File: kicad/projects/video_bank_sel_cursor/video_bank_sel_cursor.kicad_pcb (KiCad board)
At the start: 2 copper layers, 203.2 x 97.8 mm, 28 parts, among them J1 peripheral_addr_bus_connector, J2 peripheral_aux_connector, J3 peripheral_membank_connector, J4 Conn_01x16_Socket, J5 Conn_01x16_Socket, J6 Conn_01x16_Socket, J7 Conn_01x16_Socket, U1 74HC245, U10 74HC10, U11 74HC377, U12 74HC377, U13 74HC04, U14 74HC245, U15 74HC245, U2 74HC245, U3 74HC245, U4 74HC245, U5 74HC245, U6 74HC245, U7 74HC245, U8 74HC245, U9 74HC10

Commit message: Add music planning and some extra work planning video card layouts.
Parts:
- removed J6: Conn_01x16_Socket, Connector_PinSocket_2.54mm:PinSocket_1x16_P2.54mm_Horizontal
- moved U11 2.54 mm to (188.0, 124.5)
- moved U14 2.54 mm to (246.4, 124.5)
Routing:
- net unconnected-(U12-Q7-Pad19): track 14.9 -> 16.2 mm
- net unconnected-(U12-Q3-Pad9): track 16.0 -> 17.2 mm
- net unconnected-(U12-Q1-Pad5): track 16.1 -> 17.2 mm
- net unconnected-(U12-Q5-Pad15): track 16.0 -> 17.2 mm
- net unconnected-(U12-Q0-Pad2): track 17.2 -> 18.3 mm
- net unconnected-(U12-Q2-Pad6): track 17.0 -> 17.9 mm

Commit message: Bit more tweaking and fleshing out of video circuits.
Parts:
- removed U13: 74HC04, Package_DIP:DIP-14_W7.62mm_Socket
- added C10: C, Capacitor_THT:C_Disc_D5.0mm_W2.5mm_P5.00mm, F.Cu at (185.4, 133.3)
- added C11: C, Capacitor_THT:C_Disc_D5.0mm_W2.5mm_P5.00mm, F.Cu at (172.7, 133.3)
- added C12: C, Capacitor_THT:C_Disc_D5.0mm_W2.5mm_P5.00mm, F.Cu at (200.7, 133.3)
- added C13: C, Capacitor_THT:C_Disc_D5.0mm_W2.5mm_P5.00mm, F.Cu at (213.4, 133.3)
- added C14: C, Capacitor_THT:C_Disc_D5.0mm_W2.5mm_P5.00mm, F.Cu at (226.1, 128.3)
- added C15: C, Capacitor_THT:C_Disc_D5.0mm_W2.5mm_P5.00mm, F.Cu at (238.8, 128.3)
- added C2: C, Capacitor_THT:C_Disc_D5.0mm_W2.5mm_P5.00mm, F.Cu at (-14.4, 59.5)
- added C3: C, Capacitor_THT:C_Disc_D5.0mm_W2.5mm_P5.00mm, F.Cu at (-14.4, 63.6)
- added C4: C, Capacitor_THT:C_Disc_D5.0mm_W2.5mm_P5.00mm, F.Cu at (-14.4, 67.6)
- added C5: C, Capacitor_THT:C_Disc_D5.0mm_W2.5mm_P5.00mm, F.Cu at (-14.4, 71.7)
- added C6: C, Capacitor_THT:C_Disc_D5.0mm_W2.5mm_P5.00mm, F.Cu at (-14.4, 75.7)
- added C7: C, Capacitor_THT:C_Disc_D5.0mm_W2.5mm_P5.00mm, F.Cu at (-14.4, 79.8)
- added C8: C, Capacitor_THT:C_Disc_D5.0mm_W2.5mm_P5.00mm, F.Cu at (147.3, 133.3)
- added C9: C, Capacitor_THT:C_Disc_D5.0mm_W2.5mm_P5.00mm, F.Cu at (160.0, 133.3)
- moved U2 127.7 mm to (221.0, 124.5), turned to 180 degrees
- moved U6 112.1 mm to (208.3, 124.5), turned to 180 degrees
- moved U7 111.1 mm to (99.1, 104.1), turned to 90 degrees
- moved J4 109.2 mm to (139.7, 61.0)
- moved J7 106.7 mm to (248.9, 61.0)
- moved U3 67.1 mm to (99.1, 91.4), turned to 90 degrees
- moved U12 53.3 mm to (180.3, 124.5)
- moved U4 53.3 mm to (167.6, 124.5)
- moved U15 50.8 mm to (193.0, 124.5)
- moved U11 45.7 mm to (233.7, 124.5)
- moved U8 17.8 mm to (154.9, 124.5)
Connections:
- J1 pad 1: /DATA_BUS_00 -> /DATA_BUS_0
- J1 pad 10: /DATA_BUS_09 -> unconnected-(J1-D_09-Pad10)
- J1 pad 11: /DATA_BUS_10 -> unconnected-(J1-D_10-Pad11)
- J1 pad 12: /DATA_BUS_11 -> unconnected-(J1-D_11-Pad12)
- J1 pad 13: /DATA_BUS_12 -> unconnected-(J1-D_12-Pad13)
- J1 pad 14: /DATA_BUS_13 -> unconnected-(J1-D_13-Pad14)
- J1 pad 15: /DATA_BUS_14 -> unconnected-(J1-D_14-Pad15)
- J1 pad 16: /DATA_BUS_15 -> unconnected-(J1-D_15-Pad16)
- J1 pad 17: /ADDR_BUS_00 -> unconnected-(J1-A_00-Pad17)
- J1 pad 18: /ADDR_BUS_01 -> unconnected-(J1-A_01-Pad18)
- J1 pad 19: /ADDR_BUS_02 -> unconnected-(J1-A_02-Pad19)
- J1 pad 2: /DATA_BUS_01 -> /DATA_BUS_1
- J1 pad 20: /ADDR_BUS_03 -> unconnected-(J1-A_03-Pad20)
- J1 pad 21: /ADDR_BUS_04 -> unconnected-(J1-A_04-Pad21)
- J1 pad 22: /ADDR_BUS_05 -> unconnected-(J1-A_05-Pad22)
- J1 pad 23: /ADDR_BUS_06 -> unconnected-(J1-A_06-Pad23)
- J1 pad 24: /ADDR_BUS_07 -> unconnected-(J1-A_07-Pad24)
- J1 pad 25: /ADDR_BUS_08 -> unconnected-(J1-A_08-Pad25)
- J1 pad 26: /ADDR_BUS_09 -> unconnected-(J1-A_09-Pad26)
- J1 pad 27: /ADDR_BUS_10 -> unconnected-(J1-A_10-Pad27)
- J1 pad 28: /ADDR_BUS_11 -> unconnected-(J1-A_11-Pad28)
- J1 pad 29: /ADDR_BUS_12 -> unconnected-(J1-A_12-Pad29)
- J1 pad 3: /DATA_BUS_02 -> /DATA_BUS_2
- J1 pad 30: /ADDR_BUS_13 -> unconnected-(J1-A_13-Pad30)
- J1 pad 31: /ADDR_BUS_14 -> unconnected-(J1-A_14-Pad31)
- J1 pad 32: /ADDR_BUS_15 -> unconnected-(J1-A_15-Pad32)
- J1 pad 4: /DATA_BUS_03 -> /DATA_BUS_3
- J1 pad 5: /DATA_BUS_04 -> /DATA_BUS_4
- J1 pad 6: /DATA_BUS_05 -> /DATA_BUS_5
- J1 pad 7: /DATA_BUS_06 -> /DATA_BUS_6
- J1 pad 8: /DATA_BUS_07 -> /DATA_BUS_7
- J1 pad 9: /DATA_BUS_08 -> unconnected-(J1-D_08-Pad9)
- J2 pad 10: /RFM -> /MEM_ACT
- J2 pad 12: /WTM -> /~{RFM}/WTM
- J3 pad 1: /BANK_BUS_00 -> unconnected-(J3-B_00-Pad1)
- J3 pad 10: /BANK_BUS_09 -> unconnected-(J3-B_09-Pad10)
- J3 pad 11: /BANK_BUS_10 -> unconnected-(J3-B_10-Pad11)
- J3 pad 12: /BANK_BUS_11 -> unconnected-(J3-B_11-Pad12)
- J3 pad 13: /BANK_BUS_12 -> unconnected-(J3-B_12-Pad13)
- J3 pad 14: /BANK_BUS_13 -> unconnected-(J3-B_13-Pad14)
- J3 pad 15: /BANK_BUS_14 -> unconnected-(J3-B_14-Pad15)
- J3 pad 16: /BANK_BUS_15 -> unconnected-(J3-B_15-Pad16)
- J3 pad 2: /BANK_BUS_01 -> unconnected-(J3-B_01-Pad2)
- J3 pad 3: /BANK_BUS_02 -> unconnected-(J3-B_02-Pad3)
- J3 pad 4: /BANK_BUS_03 -> unconnected-(J3-B_03-Pad4)
- J3 pad 5: /BANK_BUS_04 -> unconnected-(J3-B_04-Pad5)
- J3 pad 6: /BANK_BUS_05 -> unconnected-(J3-B_05-Pad6)
- J3 pad 7: /BANK_BUS_06 -> unconnected-(J3-B_06-Pad7)
- J3 pad 8: /BANK_BUS_07 -> unconnected-(J3-B_07-Pad8)
- J3 pad 9: /BANK_BUS_08 -> unconnected-(J3-B_08-Pad9)
- J4 pad 1: unconnected-(J4-Pin_1-Pad1) -> /EXT_COL_0
- J4 pad 10: unconnected-(J4-Pin_10-Pad10) -> /EXT_ROW_1
- J4 pad 11: unconnected-(J4-Pin_11-Pad11) -> /EXT_ROW_2
- J4 pad 12: unconnected-(J4-Pin_12-Pad12) -> /EXT_ROW_3
- J4 pad 13: unconnected-(J4-Pin_13-Pad13) -> /EXT_ROW_4
- J4 pad 14: unconnected-(J4-Pin_14-Pad14) -> /EXT_ROW_5
- J4 pad 15: unconnected-(J4-Pin_15-Pad15) -> /EXT_ROW_6
- J4 pad 16: unconnected-(J4-Pin_16-Pad16) -> /EXT_ROW_7
- J4 pad 2: unconnected-(J4-Pin_2-Pad2) -> /EXT_COL_1
- J4 pad 3: unconnected-(J4-Pin_3-Pad3) -> /EXT_COL_2
- J4 pad 4: unconnected-(J4-Pin_4-Pad4) -> /EXT_COL_3
- J4 pad 5: unconnected-(J4-Pin_5-Pad5) -> /EXT_COL_4
- J4 pad 6: unconnected-(J4-Pin_6-Pad6) -> /EXT_COL_5
- J4 pad 7: unconnected-(J4-Pin_7-Pad7) -> /EXT_COL_6
- J4 pad 8: unconnected-(J4-Pin_8-Pad8) -> /EXT_COL_7
- J4 pad 9: unconnected-(J4-Pin_9-Pad9) -> /EXT_ROW_0
- J5 pad 1: unconnected-(J5-Pin_1-Pad1) -> /OUT_A_COL_0
- J5 pad 10: unconnected-(J5-Pin_10-Pad10) -> /OUT_A_ROW_1
- J5 pad 11: unconnected-(J5-Pin_11-Pad11) -> /OUT_A_ROW_2
- J5 pad 12: unconnected-(J5-Pin_12-Pad12) -> /OUT_A_ROW_3
- J5 pad 13: unconnected-(J5-Pin_13-Pad13) -> /OUT_A_ROW_4
- J5 pad 14: unconnected-(J5-Pin_14-Pad14) -> /OUT_A_ROW_5
- J5 pad 15: unconnected-(J5-Pin_15-Pad15) -> /OUT_A_ROW_6
- J5 pad 16: unconnected-(J5-Pin_16-Pad16) -> /OUT_A_ROW_7
- J5 pad 2: unconnected-(J5-Pin_2-Pad2) -> /OUT_A_COL_1
- J5 pad 3: unconnected-(J5-Pin_3-Pad3) -> /OUT_A_COL_2
- J5 pad 4: unconnected-(J5-Pin_4-Pad4) -> /OUT_A_COL_3
- J5 pad 5: unconnected-(J5-Pin_5-Pad5) -> /OUT_A_COL_4
- J5 pad 6: unconnected-(J5-Pin_6-Pad6) -> /OUT_A_COL_5
- J5 pad 7: unconnected-(J5-Pin_7-Pad7) -> /OUT_A_COL_6
- J5 pad 8: unconnected-(J5-Pin_8-Pad8) -> /OUT_A_COL_7
- J5 pad 9: unconnected-(J5-Pin_9-Pad9) -> /OUT_A_ROW_0
- J7 pad 1: unconnected-(J7-Pin_1-Pad1) -> /OUT_B_COL_0
- J7 pad 10: unconnected-(J7-Pin_10-Pad10) -> /OUT_B_ROW_1
- J7 pad 11: unconnected-(J7-Pin_11-Pad11) -> /OUT_B_ROW_2
- J7 pad 12: unconnected-(J7-Pin_12-Pad12) -> /OUT_B_ROW_3
- J7 pad 13: unconnected-(J7-Pin_13-Pad13) -> /OUT_B_ROW_4
- J7 pad 14: unconnected-(J7-Pin_14-Pad14) -> /OUT_B_ROW_5
- J7 pad 15: unconnected-(J7-Pin_15-Pad15) -> /OUT_B_ROW_6
- J7 pad 16: unconnected-(J7-Pin_16-Pad16) -> /OUT_B_ROW_7
- J7 pad 2: unconnected-(J7-Pin_2-Pad2) -> /OUT_B_COL_1
- J7 pad 3: unconnected-(J7-Pin_3-Pad3) -> /OUT_B_COL_2
- J7 pad 4: unconnected-(J7-Pin_4-Pad4) -> /OUT_B_COL_3
- J7 pad 5: unconnected-(J7-Pin_5-Pad5) -> /OUT_B_COL_4
- J7 pad 6: unconnected-(J7-Pin_6-Pad6) -> /OUT_B_COL_5
- J7 pad 7: unconnected-(J7-Pin_7-Pad7) -> /OUT_B_COL_6
- J7 pad 8: unconnected-(J7-Pin_8-Pad8) -> /OUT_B_COL_7
- J7 pad 9: unconnected-(J7-Pin_9-Pad9) -> /OUT_B_ROW_0
- U1 pad 10: unconnected-(U1-GND-Pad10) -> GND
- U1 pad 11: unconnected-(U1-B8-Pad11) -> /OUT_A_ROW_7
- U1 pad 12: unconnected-(U1-B7-Pad12) -> /OUT_A_ROW_6
- U1 pad 13: unconnected-(U1-B6-Pad13) -> /OUT_A_ROW_5
- U1 pad 14: unconnected-(U1-B5-Pad14) -> /OUT_A_ROW_4
- U1 pad 15: unconnected-(U1-B4-Pad15) -> /OUT_A_ROW_3
- U1 pad 16: unconnected-(U1-B3-Pad16) -> /OUT_A_ROW_2
- U1 pad 17: unconnected-(U1-B2-Pad17) -> /OUT_A_ROW_1
- U1 pad 18: unconnected-(U1-B1-Pad18) -> /OUT_A_ROW_0
- U1 pad 19: unconnected-(U1-~{OE}-Pad19) -> /~{BANK_SEL}
- U1 pad 2: unconnected-(U1-A1-Pad2) -> /EXT_ROW_0
- U1 pad 20: unconnected-(U1-VCC-Pad20) -> VCC
- U1 pad 3: unconnected-(U1-A2-Pad3) -> /EXT_ROW_1
- U1 pad 4: unconnected-(U1-A3-Pad4) -> /EXT_ROW_2
- U1 pad 5: unconnected-(U1-A3-Pad5) -> /EXT_ROW_3
- U1 pad 6: unconnected-(U1-A5-Pad6) -> /EXT_ROW_4
- U1 pad 7: unconnected-(U1-A6-Pad7) -> /EXT_ROW_5
- U1 pad 8: unconnected-(U1-A7-Pad8) -> /EXT_ROW_6
- U1 pad 9: unconnected-(U1-A8-Pad9) -> /EXT_ROW_7
- U10 pad 1: unconnected-(U10-Pad1) -> /CURSOR_ROW_ADDRESSED
- U10 pad 10: unconnected-(U10-Pad10) -> VCC
- U10 pad 11: unconnected-(U10-Pad11) -> VCC
- U10 pad 12: unconnected-(U10-Pad12) -> /~{CURSOR_ROW_WTM}
- U10 pad 13: unconnected-(U10-Pad13) -> /~{RFM}/WTM
- U10 pad 14: unconnected-(U10D-VCC-Pad14) -> VCC
- U10 pad 2: unconnected-(U10-Pad2) -> /MEM_ACT
- U10 pad 3: unconnected-(U10-Pad3) -> /CURSOR_COL_ADDRESSED
- U10 pad 4: unconnected-(U10-Pad4) -> /MEM_ACT
- U10 pad 5: unconnected-(U10-Pad5) -> /RFM/~{WTM}
- U10 pad 6: unconnected-(U10-Pad6) -> /~{CURSOR_COL_RFM}
- U10 pad 7: unconnected-(U10D-GND-Pad7) -> GND
- U10 pad 8: unconnected-(U10-Pad8) -> /~{BANK_SEL}
- U10 pad 9: unconnected-(U10-Pad9) -> /BANK_SEL
- U11 pad 1: unconnected-(U11-~{E}-Pad1) -> /~{CURSOR_ROW_WTM}
- U11 pad 10: unconnected-(U11-GND-Pad10) -> GND
- U11 pad 11: unconnected-(U11-CP-Pad11) -> /DATA_CLK
- U11 pad 12: unconnected-(U11-Q4-Pad12) -> /CURS_ROW_4
- U11 pad 13: unconnected-(U11-D4-Pad13) -> /DATA_BUS_4
- U11 pad 14: unconnected-(U11-D5-Pad14) -> /DATA_BUS_5
- U11 pad 15: unconnected-(U11-Q5-Pad15) -> /CURS_ROW_5
- U11 pad 16: unconnected-(U11-Q6-Pad16) -> /CURS_ROW_6
- U11 pad 17: unconnected-(U11-D6-Pad17) -> /DATA_BUS_6
- U11 pad 18: unconnected-(U11-D7-Pad18) -> /DATA_BUS_7
- U11 pad 19: unconnected-(U11-Q7-Pad19) -> /CURS_ROW_7
- U11 pad 2: unconnected-(U11-Q0-Pad2) -> /CURS_ROW_0
- U11 pad 20: unconnected-(U11-VCC-Pad20) -> VCC
- U11 pad 3: unconnected-(U11-D0-Pad3) -> /DATA_BUS_0
- U11 pad 4: unconnected-(U11-D1-Pad4) -> /DATA_BUS_1
- U11 pad 5: unconnected-(U11-Q1-Pad5) -> /CURS_ROW_1
- U11 pad 6: unconnected-(U11-Q2-Pad6) -> /CURS_ROW_2
- U11 pad 7: unconnected-(U11-D2-Pad7) -> /DATA_BUS_2
- U11 pad 8: unconnected-(U11-D3-Pad8) -> /DATA_BUS_3
- U11 pad 9: unconnected-(U11-Q3-Pad9) -> /CURS_ROW_3
- U12 pad 1: unconnected-(U12-~{E}-Pad1) -> /~{CURSOR_COL_WTM}
- U12 pad 10: unconnected-(U12-GND-Pad10) -> GND
- U12 pad 11: unconnected-(U12-CP-Pad11) -> /DATA_CLK
- U12 pad 12: unconnected-(U12-Q4-Pad12) -> /CURS_COL_4
- U12 pad 13: unconnected-(U12-D4-Pad13) -> /DATA_BUS_4
- U12 pad 14: unconnected-(U12-D5-Pad14) -> /DATA_BUS_5
- U12 pad 15: unconnected-(U12-Q5-Pad15) -> /CURS_COL_5
- U12 pad 16: unconnected-(U12-Q6-Pad16) -> /CURS_COL_6
- U12 pad 17: unconnected-(U12-D6-Pad17) -> /DATA_BUS_6
- U12 pad 18: unconnected-(U12-D7-Pad18) -> /DATA_BUS_7
- U12 pad 19: unconnected-(U12-Q7-Pad19) -> /CURS_COL_7
- U12 pad 2: unconnected-(U12-Q0-Pad2) -> /CURS_COL_0
- U12 pad 20: unconnected-(U12-VCC-Pad20) -> VCC
- U12 pad 3: unconnected-(U12-D0-Pad3) -> /DATA_BUS_0
- U12 pad 4: unconnected-(U12-D1-Pad4) -> /DATA_BUS_1
- U12 pad 5: unconnected-(U12-Q1-Pad5) -> /CURS_COL_1
- U12 pad 6: unconnected-(U12-Q2-Pad6) -> /CURS_COL_2
- U12 pad 7: unconnected-(U12-D2-Pad7) -> /DATA_BUS_2
- U12 pad 8: unconnected-(U12-D3-Pad8) -> /DATA_BUS_3
- U12 pad 9: unconnected-(U12-Q3-Pad9) -> /CURS_COL_3
- U14 pad 10: unconnected-(U14-GND-Pad10) -> GND
- U14 pad 11: unconnected-(U14-B8-Pad11) -> /DATA_BUS_7
- U14 pad 12: unconnected-(U14-B7-Pad12) -> /DATA_BUS_6
- U14 pad 13: unconnected-(U14-B6-Pad13) -> /DATA_BUS_5
- U14 pad 14: unconnected-(U14-B5-Pad14) -> /DATA_BUS_4
- U14 pad 15: unconnected-(U14-B4-Pad15) -> /DATA_BUS_3
- U14 pad 16: unconnected-(U14-B3-Pad16) -> /DATA_BUS_2
- U14 pad 17: unconnected-(U14-B2-Pad17) -> /DATA_BUS_1
- U14 pad 18: unconnected-(U14-B1-Pad18) -> /DATA_BUS_0
- U14 pad 19: unconnected-(U14-~{OE}-Pad19) -> /~{CURSOR_ROW_RFM}
- U14 pad 2: unconnected-(U14-A1-Pad2) -> /CURS_ROW_0
- U14 pad 20: unconnected-(U14-VCC-Pad20) -> VCC
- U14 pad 3: unconnected-(U14-A2-Pad3) -> /CURS_ROW_1
- U14 pad 4: unconnected-(U14-A3-Pad4) -> /CURS_ROW_2
- U14 pad 5: unconnected-(U14-A3-Pad5) -> /CURS_ROW_3
- U14 pad 6: unconnected-(U14-A5-Pad6) -> /CURS_ROW_4
- U14 pad 7: unconnected-(U14-A6-Pad7) -> /CURS_ROW_5
- U14 pad 8: unconnected-(U14-A7-Pad8) -> /CURS_ROW_6
- U14 pad 9: unconnected-(U14-A8-Pad9) -> /CURS_ROW_7
- U15 pad 10: unconnected-(U15-GND-Pad10) -> GND
- U15 pad 11: unconnected-(U15-B8-Pad11) -> /DATA_BUS_7
- U15 pad 12: unconnected-(U15-B7-Pad12) -> /DATA_BUS_6
- U15 pad 13: unconnected-(U15-B6-Pad13) -> /DATA_BUS_5
- U15 pad 14: unconnected-(U15-B5-Pad14) -> /DATA_BUS_4
- U15 pad 15: unconnected-(U15-B4-Pad15) -> /DATA_BUS_3
- U15 pad 16: unconnected-(U15-B3-Pad16) -> /DATA_BUS_2
- U15 pad 17: unconnected-(U15-B2-Pad17) -> /DATA_BUS_1
- U15 pad 18: unconnected-(U15-B1-Pad18) -> /DATA_BUS_0
- U15 pad 19: unconnected-(U15-~{OE}-Pad19) -> /~{CURSOR_COL_RFM}
- U15 pad 2: unconnected-(U15-A1-Pad2) -> /CURS_COL_0
- U15 pad 20: unconnected-(U15-VCC-Pad20) -> VCC
- U15 pad 3: unconnected-(U15-A2-Pad3) -> /CURS_COL_1
- U15 pad 4: unconnected-(U15-A3-Pad4) -> /CURS_COL_2
- U15 pad 5: unconnected-(U15-A3-Pad5) -> /CURS_COL_3
- U15 pad 6: unconnected-(U15-A5-Pad6) -> /CURS_COL_4
- U15 pad 7: unconnected-(U15-A6-Pad7) -> /CURS_COL_5
- U15 pad 8: unconnected-(U15-A7-Pad8) -> /CURS_COL_6
- U15 pad 9: unconnected-(U15-A8-Pad9) -> /CURS_COL_7
- U2 pad 10: unconnected-(U2-GND-Pad10) -> GND
- U2 pad 11: unconnected-(U2-B8-Pad11) -> /OUT_A_ROW_7
- U2 pad 12: unconnected-(U2-B7-Pad12) -> /OUT_A_ROW_6
- U2 pad 13: unconnected-(U2-B6-Pad13) -> /OUT_A_ROW_5
- U2 pad 14: unconnected-(U2-B5-Pad14) -> /OUT_A_ROW_4
- U2 pad 15: unconnected-(U2-B4-Pad15) -> /OUT_A_ROW_3
- U2 pad 16: unconnected-(U2-B3-Pad16) -> /OUT_A_ROW_2
- U2 pad 17: unconnected-(U2-B2-Pad17) -> /OUT_A_ROW_1
- U2 pad 18: unconnected-(U2-B1-Pad18) -> /OUT_A_ROW_0
- U2 pad 19: unconnected-(U2-~{OE}-Pad19) -> /BANK_SEL
- U2 pad 2: unconnected-(U2-A1-Pad2) -> /CURS_ROW_0
- U2 pad 20: unconnected-(U2-VCC-Pad20) -> VCC
- U2 pad 3: unconnected-(U2-A2-Pad3) -> /CURS_ROW_1
- U2 pad 4: unconnected-(U2-A3-Pad4) -> /CURS_ROW_2
- U2 pad 5: unconnected-(U2-A3-Pad5) -> /CURS_ROW_3
- U2 pad 6: unconnected-(U2-A5-Pad6) -> /CURS_ROW_4
- U2 pad 7: unconnected-(U2-A6-Pad7) -> /CURS_ROW_5
- U2 pad 8: unconnected-(U2-A7-Pad8) -> /CURS_ROW_6
- U2 pad 9: unconnected-(U2-A8-Pad9) -> /CURS_ROW_7
- U3 pad 10: unconnected-(U3-GND-Pad10) -> GND
- U3 pad 11: unconnected-(U3-B8-Pad11) -> /OUT_A_COL_7
- U3 pad 12: unconnected-(U3-B7-Pad12) -> /OUT_A_COL_6
- U3 pad 13: unconnected-(U3-B6-Pad13) -> /OUT_A_COL_5
- U3 pad 14: unconnected-(U3-B5-Pad14) -> /OUT_A_COL_4
- U3 pad 15: unconnected-(U3-B4-Pad15) -> /OUT_A_COL_3
- U3 pad 16: unconnected-(U3-B3-Pad16) -> /OUT_A_COL_2
- U3 pad 17: unconnected-(U3-B2-Pad17) -> /OUT_A_COL_1
- U3 pad 18: unconnected-(U3-B1-Pad18) -> /OUT_A_COL_0
- U3 pad 19: unconnected-(U3-~{OE}-Pad19) -> /~{BANK_SEL}
- U3 pad 2: unconnected-(U3-A1-Pad2) -> /EXT_COL_0
- U3 pad 20: unconnected-(U3-VCC-Pad20) -> VCC
- U3 pad 3: unconnected-(U3-A2-Pad3) -> /EXT_COL_1
- U3 pad 4: unconnected-(U3-A3-Pad4) -> /EXT_COL_2
- U3 pad 5: unconnected-(U3-A3-Pad5) -> /EXT_COL_3
- U3 pad 6: unconnected-(U3-A5-Pad6) -> /EXT_COL_4
- U3 pad 7: unconnected-(U3-A6-Pad7) -> /EXT_COL_5
- U3 pad 8: unconnected-(U3-A7-Pad8) -> /EXT_COL_6
- U3 pad 9: unconnected-(U3-A8-Pad9) -> /EXT_COL_7
- U4 pad 10: unconnected-(U4-GND-Pad10) -> GND
- U4 pad 11: unconnected-(U4-B8-Pad11) -> /OUT_A_COL_7
- U4 pad 12: unconnected-(U4-B7-Pad12) -> /OUT_A_COL_6
- U4 pad 13: unconnected-(U4-B6-Pad13) -> /OUT_A_COL_5
- U4 pad 14: unconnected-(U4-B5-Pad14) -> /OUT_A_COL_4
- U4 pad 15: unconnected-(U4-B4-Pad15) -> /OUT_A_COL_3
- U4 pad 16: unconnected-(U4-B3-Pad16) -> /OUT_A_COL_2
- U4 pad 17: unconnected-(U4-B2-Pad17) -> /OUT_A_COL_1
- U4 pad 18: unconnected-(U4-B1-Pad18) -> /OUT_A_COL_0
- U4 pad 19: unconnected-(U4-~{OE}-Pad19) -> /BANK_SEL
- U4 pad 2: unconnected-(U4-A1-Pad2) -> /CURS_COL_0
- U4 pad 20: unconnected-(U4-VCC-Pad20) -> VCC
- U4 pad 3: unconnected-(U4-A2-Pad3) -> /CURS_COL_1
- U4 pad 4: unconnected-(U4-A3-Pad4) -> /CURS_COL_2
- U4 pad 5: unconnected-(U4-A3-Pad5) -> /CURS_COL_3
- U4 pad 6: unconnected-(U4-A5-Pad6) -> /CURS_COL_4
- U4 pad 7: unconnected-(U4-A6-Pad7) -> /CURS_COL_5
- U4 pad 8: unconnected-(U4-A7-Pad8) -> /CURS_COL_6
- U4 pad 9: unconnected-(U4-A8-Pad9) -> /CURS_COL_7
- U5 pad 10: unconnected-(U5-GND-Pad10) -> GND
- U5 pad 11: unconnected-(U5-B8-Pad11) -> /OUT_B_ROW_7
- U5 pad 12: unconnected-(U5-B7-Pad12) -> /OUT_B_ROW_6
- U5 pad 13: unconnected-(U5-B6-Pad13) -> /OUT_B_ROW_5
- U5 pad 14: unconnected-(U5-B5-Pad14) -> /OUT_B_ROW_4
- U5 pad 15: unconnected-(U5-B4-Pad15) -> /OUT_B_ROW_3
- U5 pad 16: unconnected-(U5-B3-Pad16) -> /OUT_B_ROW_2
- U5 pad 17: unconnected-(U5-B2-Pad17) -> /OUT_B_ROW_1
- U5 pad 18: unconnected-(U5-B1-Pad18) -> /OUT_B_ROW_0
- U5 pad 19: unconnected-(U5-~{OE}-Pad19) -> /BANK_SEL
- U5 pad 2: unconnected-(U5-A1-Pad2) -> /EXT_ROW_0
- U5 pad 20: unconnected-(U5-VCC-Pad20) -> VCC
- U5 pad 3: unconnected-(U5-A2-Pad3) -> /EXT_ROW_1
- U5 pad 4: unconnected-(U5-A3-Pad4) -> /EXT_ROW_2
- U5 pad 5: unconnected-(U5-A3-Pad5) -> /EXT_ROW_3
- U5 pad 6: unconnected-(U5-A5-Pad6) -> /EXT_ROW_4
- U5 pad 7: unconnected-(U5-A6-Pad7) -> /EXT_ROW_5
- U5 pad 8: unconnected-(U5-A7-Pad8) -> /EXT_ROW_6
- U5 pad 9: unconnected-(U5-A8-Pad9) -> /EXT_ROW_7
- U6 pad 10: unconnected-(U6-GND-Pad10) -> GND
- U6 pad 11: unconnected-(U6-B8-Pad11) -> /OUT_B_ROW_7
- U6 pad 12: unconnected-(U6-B7-Pad12) -> /OUT_B_ROW_6
- U6 pad 13: unconnected-(U6-B6-Pad13) -> /OUT_B_ROW_5
- U6 pad 14: unconnected-(U6-B5-Pad14) -> /OUT_B_ROW_4
- U6 pad 15: unconnected-(U6-B4-Pad15) -> /OUT_B_ROW_3
- U6 pad 16: unconnected-(U6-B3-Pad16) -> /OUT_B_ROW_2
- U6 pad 17: unconnected-(U6-B2-Pad17) -> /OUT_B_ROW_1
- U6 pad 18: unconnected-(U6-B1-Pad18) -> /OUT_B_ROW_0
- U6 pad 19: unconnected-(U6-~{OE}-Pad19) -> /~{BANK_SEL}
- U6 pad 2: unconnected-(U6-A1-Pad2) -> /CURS_ROW_0
- U6 pad 20: unconnected-(U6-VCC-Pad20) -> VCC
- U6 pad 3: unconnected-(U6-A2-Pad3) -> /CURS_ROW_1
- U6 pad 4: unconnected-(U6-A3-Pad4) -> /CURS_ROW_2
- U6 pad 5: unconnected-(U6-A3-Pad5) -> /CURS_ROW_3
- U6 pad 6: unconnected-(U6-A5-Pad6) -> /CURS_ROW_4
- U6 pad 7: unconnected-(U6-A6-Pad7) -> /CURS_ROW_5
- U6 pad 8: unconnected-(U6-A7-Pad8) -> /CURS_ROW_6
- U6 pad 9: unconnected-(U6-A8-Pad9) -> /CURS_ROW_7
- U7 pad 10: unconnected-(U7-GND-Pad10) -> GND
- U7 pad 11: unconnected-(U7-B8-Pad11) -> /OUT_B_COL_7
- U7 pad 12: unconnected-(U7-B7-Pad12) -> /OUT_B_COL_6
- U7 pad 13: unconnected-(U7-B6-Pad13) -> /OUT_B_COL_5
- U7 pad 14: unconnected-(U7-B5-Pad14) -> /OUT_B_COL_4
- U7 pad 15: unconnected-(U7-B4-Pad15) -> /OUT_B_COL_3
- U7 pad 16: unconnected-(U7-B3-Pad16) -> /OUT_B_COL_2
- U7 pad 17: unconnected-(U7-B2-Pad17) -> /OUT_B_COL_1
- U7 pad 18: unconnected-(U7-B1-Pad18) -> /OUT_B_COL_0
- U7 pad 19: unconnected-(U7-~{OE}-Pad19) -> /BANK_SEL
- U7 pad 2: unconnected-(U7-A1-Pad2) -> /EXT_COL_0
- U7 pad 20: unconnected-(U7-VCC-Pad20) -> VCC
- U7 pad 3: unconnected-(U7-A2-Pad3) -> /EXT_COL_1
- U7 pad 4: unconnected-(U7-A3-Pad4) -> /EXT_COL_2
- U7 pad 5: unconnected-(U7-A3-Pad5) -> /EXT_COL_3
- U7 pad 6: unconnected-(U7-A5-Pad6) -> /EXT_COL_4
- U7 pad 7: unconnected-(U7-A6-Pad7) -> /EXT_COL_5
- U7 pad 8: unconnected-(U7-A7-Pad8) -> /EXT_COL_6
- U7 pad 9: unconnected-(U7-A8-Pad9) -> /EXT_COL_7
- U8 pad 10: unconnected-(U8-GND-Pad10) -> GND
- U8 pad 11: unconnected-(U8-B8-Pad11) -> /OUT_B_COL_7
- U8 pad 12: unconnected-(U8-B7-Pad12) -> /OUT_B_COL_6
- U8 pad 13: unconnected-(U8-B6-Pad13) -> /OUT_B_COL_5
- U8 pad 14: unconnected-(U8-B5-Pad14) -> /OUT_B_COL_4
- U8 pad 15: unconnected-(U8-B4-Pad15) -> /OUT_B_COL_3
- U8 pad 16: unconnected-(U8-B3-Pad16) -> /OUT_B_COL_2
- U8 pad 17: unconnected-(U8-B2-Pad17) -> /OUT_B_COL_1
- U8 pad 18: unconnected-(U8-B1-Pad18) -> /OUT_B_COL_0
- U8 pad 19: unconnected-(U8-~{OE}-Pad19) -> /~{BANK_SEL}
- U8 pad 2: unconnected-(U8-A1-Pad2) -> /CURS_COL_0
- U8 pad 20: unconnected-(U8-VCC-Pad20) -> VCC
- U8 pad 3: unconnected-(U8-A2-Pad3) -> /CURS_COL_1
- U8 pad 4: unconnected-(U8-A3-Pad4) -> /CURS_COL_2
- U8 pad 5: unconnected-(U8-A3-Pad5) -> /CURS_COL_3
- U8 pad 6: unconnected-(U8-A5-Pad6) -> /CURS_COL_4
- U8 pad 7: unconnected-(U8-A6-Pad7) -> /CURS_COL_5
- U8 pad 8: unconnected-(U8-A7-Pad8) -> /CURS_COL_6
- U8 pad 9: unconnected-(U8-A8-Pad9) -> /CURS_COL_7
- U9 pad 1: unconnected-(U9-Pad1) -> /~{RFM}/WTM
- U9 pad 10: unconnected-(U9-Pad10) -> /MEM_ACT
- U9 pad 11: unconnected-(U9-Pad11) -> /RFM/~{WTM}
- U9 pad 12: unconnected-(U9-Pad12) -> /RFM/~{WTM}
- U9 pad 13: unconnected-(U9-Pad13) -> VCC
- U9 pad 14: unconnected-(U9D-VCC-Pad14) -> VCC
- U9 pad 2: unconnected-(U9-Pad2) -> VCC
- U9 pad 3: unconnected-(U9-Pad3) -> /CURSOR_COL_ADDRESSED
- U9 pad 4: unconnected-(U9-Pad4) -> /MEM_ACT
- U9 pad 5: unconnected-(U9-Pad5) -> /~{RFM}/WTM
- U9 pad 6: unconnected-(U9-Pad6) -> /~{CURSOR_COL_WTM}
- U9 pad 7: unconnected-(U9D-GND-Pad7) -> GND
- U9 pad 8: unconnected-(U9-Pad8) -> /~{CURSOR_ROW_RFM}
- U9 pad 9: unconnected-(U9-Pad9) -> /CURSOR_ROW_ADDRESSED
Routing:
- net (no net): track 3591.6 -> 2098.0 mm, vias 8 -> 0
- net /OUT_B_ROW_7: track 0.00 -> 87.1 mm
- net /OUT_B_ROW_6: track 0.00 -> 87.1 mm
- net /OUT_B_ROW_5: track 0.00 -> 87.1 mm
- net /OUT_B_ROW_4: track 0.00 -> 87.1 mm
- net /OUT_B_ROW_3: track 0.00 -> 87.1 mm
- net /OUT_B_ROW_2: track 0.00 -> 87.1 mm
- net /OUT_B_ROW_1: track 0.00 -> 87.1 mm
- net /OUT_B_ROW_0: track 0.00 -> 87.1 mm
- net /OUT_A_ROW_7: track 0.00 -> 87.1 mm
- net /OUT_A_ROW_6: track 0.00 -> 87.1 mm
- net /OUT_A_ROW_5: track 0.00 -> 87.1 mm
- net /OUT_A_ROW_4: track 0.00 -> 87.1 mm
- net /OUT_A_ROW_3: track 0.00 -> 87.1 mm
- net /OUT_A_ROW_2: track 0.00 -> 87.1 mm
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
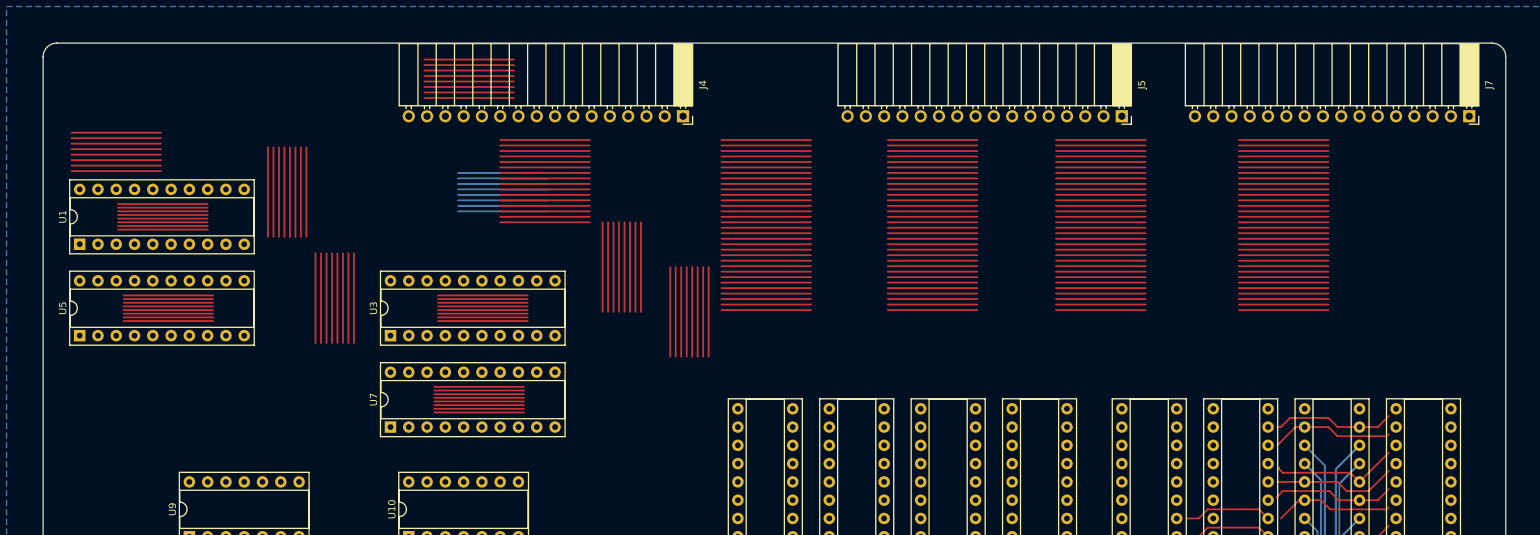
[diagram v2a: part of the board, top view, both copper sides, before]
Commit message: Adding video aux and some bits and bieces on video boards.
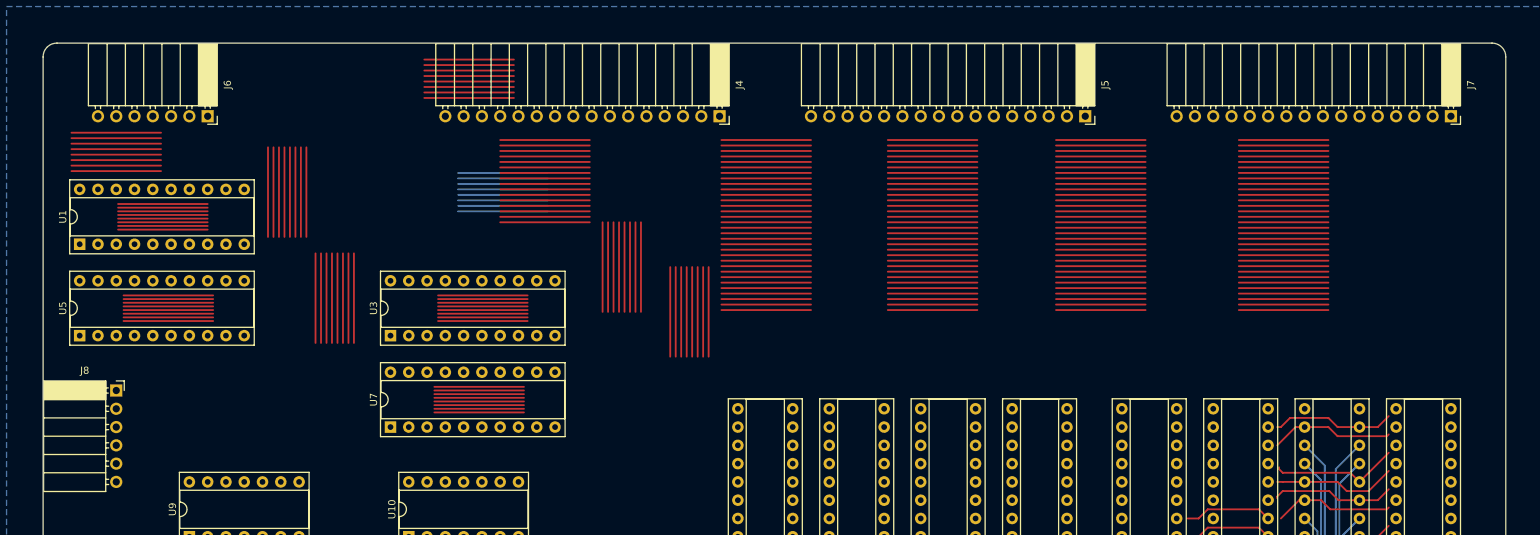
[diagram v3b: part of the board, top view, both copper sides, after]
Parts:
- added J6: video_aux, Connector_PinSocket_2.54mm:PinSocket_1x07_P2.54mm_Horizontal, F.Cu at (73.7, 61.0)
- added J8: Conn_01x06_Socket, Connector_PinSocket_2.54mm:PinSocket_1x06_P2.54mm_Horizontal, F.Cu at (61.0, 99.1)
- moved J4 5.08 mm to (144.8, 61.0)
- moved J5 5.08 mm to (195.6, 61.0)
- moved J7 2.54 mm to (246.4, 61.0)

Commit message: Start work on video bank sel cursor.
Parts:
- added R2: 10K, Resistor_THT:R_Axial_DIN0207_L6.3mm_D2.5mm_P10.16mm_Horizontal, F.Cu at (86.4, 124.5)
- added R3: 10K, Resistor_THT:R_Axial_DIN0207_L6.3mm_D2.5mm_P10.16mm_Horizontal, F.Cu at (101.6, 124.5)
- moved U14 50.0 mm to (200.7, 104.1), turned to 0 degrees
- moved U15 50.0 mm to (147.3, 104.1), turned to 0 degrees
- moved C10 39.3 mm to (195.6, 95.3), turned to -90 degrees
- moved C11 39.3 mm to (182.9, 95.3), turned to -90 degrees
- moved C12 39.3 mm to (210.8, 95.3), turned to -90 degrees
- moved C13 39.3 mm to (223.5, 95.3), turned to -90 degrees
- moved C8 39.3 mm to (157.5, 95.3), turned to -90 degrees
- moved C9 39.3 mm to (170.2, 95.3), turned to -90 degrees
- moved U6 36.6 mm to (238.8, 104.1), turned to 0 degrees
- moved U8 36.6 mm to (185.4, 104.1), turned to 0 degrees
- moved C14 29.7 mm to (236.2, 100.3), turned to 90 degrees
- moved C15 29.7 mm to (248.9, 100.3), turned to 90 degrees
- moved U11 28.7 mm to (213.4, 104.1), turned to 0 degrees
- moved U12 28.7 mm to (160.0, 104.1), turned to 0 degrees
- moved U2 20.9 mm to (226.1, 104.1), turned to 0 degrees
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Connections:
- U14 pad 11: /DATA_BUS_7 -> /CURS_ROW_4
- U14 pad 12: /DATA_BUS_6 -> /CURS_ROW_3
- U14 pad 13: /DATA_BUS_5 -> /CURS_ROW_5
- U14 pad 14: /DATA_BUS_4 -> /CURS_ROW_2
- U14 pad 15: /DATA_BUS_3 -> /CURS_ROW_6
- U14 pad 16: /DATA_BUS_2 -> /CURS_ROW_1
- U14 pad 17: /DATA_BUS_1 -> /CURS_ROW_7
- U14 pad 18: /DATA_BUS_0 -> /CURS_ROW_0
- U14 pad 2: /CURS_ROW_0 -> /DATA_BUS_0
- U14 pad 3: /CURS_ROW_1 -> /DATA_BUS_7
- U14 pad 4: /CURS_ROW_2 -> /DATA_BUS_1
- U14 pad 5: /CURS_ROW_3 -> /DATA_BUS_6
- U14 pad 6: /CURS_ROW_4 -> /DATA_BUS_2
- U14 pad 7: /CURS_ROW_5 -> /DATA_BUS_5
- U14 pad 8: /CURS_ROW_6 -> /DATA_BUS_3
- U14 pad 9: /CURS_ROW_7 -> /DATA_BUS_4
- U15 pad 11: /DATA_BUS_7 -> /CURS_COL_4
- U15 pad 12: /DATA_BUS_6 -> /CURS_COL_3
- U15 pad 13: /DATA_BUS_5 -> /CURS_COL_5
- U15 pad 14: /DATA_BUS_4 -> /CURS_COL_2
- U15 pad 15: /DATA_BUS_3 -> /CURS_COL_6
- U15 pad 16: /DATA_BUS_2 -> /CURS_COL_1
- U15 pad 17: /DATA_BUS_1 -> /CURS_COL_7
- U15 pad 18: /DATA_BUS_0 -> /CURS_COL_0
- U15 pad 2: /CURS_COL_0 -> /DATA_BUS_0
- U15 pad 3: /CURS_COL_1 -> /DATA_BUS_7
- U15 pad 4: /CURS_COL_2 -> /DATA_BUS_1
- U15 pad 5: /CURS_COL_3 -> /DATA_BUS_6
- U15 pad 6: /CURS_COL_4 -> /DATA_BUS_2
- U15 pad 7: /CURS_COL_5 -> /DATA_BUS_5
- U15 pad 8: /CURS_COL_6 -> /DATA_BUS_3
- U15 pad 9: /CURS_COL_7 -> /DATA_BUS_4
- U2 pad 11: /OUT_A_ROW_7 -> /OUT_A_ROW_4
- U2 pad 12: /OUT_A_ROW_6 -> /OUT_A_ROW_3
- U2 pad 14: /OUT_A_ROW_4 -> /OUT_A_ROW_2
- U2 pad 15: /OUT_A_ROW_3 -> /OUT_A_ROW_6
- U2 pad 16: /OUT_A_ROW_2 -> /OUT_A_ROW_1
- U2 pad 17: /OUT_A_ROW_1 -> /OUT_A_ROW_7
- U2 pad 3: /CURS_ROW_1 -> /CURS_ROW_7
- U2 pad 4: /CURS_ROW_2 -> /CURS_ROW_1
- U2 pad 5: /CURS_ROW_3 -> /CURS_ROW_6
- U2 pad 6: /CURS_ROW_4 -> /CURS_ROW_2
- U2 pad 8: /CURS_ROW_6 -> /CURS_ROW_3
- U2 pad 9: /CURS_ROW_7 -> /CURS_ROW_4
- U4 pad 11: /OUT_A_COL_7 -> /OUT_A_COL_4
- U4 pad 12: /OUT_A_COL_6 -> /OUT_A_COL_3
- U4 pad 14: /OUT_A_COL_4 -> /OUT_A_COL_2
- U4 pad 15: /OUT_A_COL_3 -> /OUT_A_COL_6
- U4 pad 16: /OUT_A_COL_2 -> /OUT_A_COL_1
- U4 pad 17: /OUT_A_COL_1 -> /OUT_A_COL_7
- U4 pad 3: /CURS_COL_1 -> /CURS_COL_7
- U4 pad 4: /CURS_COL_2 -> /CURS_COL_1
- U4 pad 5: /CURS_COL_3 -> /CURS_COL_6
- U4 pad 6: /CURS_COL_4 -> /CURS_COL_2
- U4 pad 8: /CURS_COL_6 -> /CURS_COL_3
- U4 pad 9: /CURS_COL_7 -> /CURS_COL_4
- U6 pad 11: /OUT_B_ROW_7 -> /OUT_B_ROW_4
- U6 pad 12: /OUT_B_ROW_6 -> /OUT_B_ROW_3
- U6 pad 14: /OUT_B_ROW_4 -> /OUT_B_ROW_2
- U6 pad 15: /OUT_B_ROW_3 -> /OUT_B_ROW_6
- U6 pad 16: /OUT_B_ROW_2 -> /OUT_B_ROW_1
- U6 pad 17: /OUT_B_ROW_1 -> /OUT_B_ROW_7
- U6 pad 3: /CURS_ROW_1 -> /CURS_ROW_7
- U6 pad 4: /CURS_ROW_2 -> /CURS_ROW_1
- U6 pad 5: /CURS_ROW_3 -> /CURS_ROW_6
- U6 pad 6: /CURS_ROW_4 -> /CURS_ROW_2
- U6 pad 8: /CURS_ROW_6 -> /CURS_ROW_3
- U6 pad 9: /CURS_ROW_7 -> /CURS_ROW_4
- U8 pad 11: /OUT_B_COL_7 -> /OUT_B_COL_4
- U8 pad 12: /OUT_B_COL_6 -> /OUT_B_COL_3
- U8 pad 14: /OUT_B_COL_4 -> /OUT_B_COL_2
- U8 pad 15: /OUT_B_COL_3 -> /OUT_B_COL_6
- U8 pad 16: /OUT_B_COL_2 -> /OUT_B_COL_1
- U8 pad 17: /OUT_B_COL_1 -> /OUT_B_COL_7
- U8 pad 3: /CURS_COL_1 -> /CURS_COL_7
- U8 pad 4: /CURS_COL_2 -> /CURS_COL_1
- U8 pad 5: /CURS_COL_3 -> /CURS_COL_6
- U8 pad 6: /CURS_COL_4 -> /CURS_COL_2
- U8 pad 8: /CURS_COL_6 -> /CURS_COL_3
- U8 pad 9: /CURS_COL_7 -> /CURS_COL_4
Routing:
- net (no net): track 2098.0 -> 99.6 mm
- net VCC: track 0.00 -> 180.0 mm, vias 0 -> 8
- net /OUT_B_ROW_4: track 87.1 -> 199.5 mm, vias 0 -> 3
- net /OUT_B_ROW_6: track 87.1 -> 199.2 mm, vias 0 -> 3
- net /OUT_B_ROW_2: track 87.1 -> 198.5 mm, vias 0 -> 3
- net /OUT_B_ROW_3: track 87.1 -> 198.5 mm, vias 0 -> 3
- net /OUT_B_COL_4: track 74.7 -> 185.8 mm, vias 0 -> 3
- net /OUT_B_ROW_5: track 87.1 -> 198.0 mm, vias 0 -> 3
- net /OUT_B_COL_3: track 74.7 -> 185.0 mm, vias 0 -> 3
- net /OUT_B_ROW_1: track 87.1 -> 196.0 mm, vias 0 -> 3
- net /OUT_B_ROW_7: track 87.1 -> 195.0 mm, vias 0 -> 1
- net /OUT_B_COL_2: track 74.7 -> 182.5 mm, vias 0 -> 3
- net /OUT_B_COL_0: track 74.7 -> 182.0 mm, vias 0 -> 3
- net /OUT_B_COL_1: track 74.7 -> 180.8 mm, vias 0 -> 3
- net /OUT_B_ROW_0: track 87.1 -> 191.7 mm, vias 0 -> 1
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
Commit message: Add indicator LEDs to shift status delay board. Bit of work on bank sel PCB.
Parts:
- moved C6 121.8 mm to (100.3, 116.8), turned to 90 degrees
- moved C5 118.5 mm to (100.3, 101.5), turned to 90 degrees
- moved C4 116.7 mm to (100.3, 88.8), turned to 90 degrees
- moved C7 92.0 mm to (69.8, 116.8), turned to 90 degrees
- moved C3 73.5 mm to (54.6, 88.8), turned to 90 degrees
- moved C2 71.0 mm to (54.6, 76.1), turned to 90 degrees
- moved U3 5.08 mm to (104.1, 91.4)
- moved U7 5.08 mm to (104.1, 104.1)
- moved R2 2.54 mm to (88.9, 124.5)
- moved R3 2.54 mm to (104.1, 124.5)
- moved U10 2.54 mm to (104.1, 119.4)
- moved U1 2.54 mm to (58.4, 78.7)
- moved U5 2.54 mm to (58.4, 91.4)
- moved U9 2.54 mm to (73.7, 119.4)
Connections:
- U1 pad 11: /OUT_A_ROW_7 -> /EXT_ROW_7
- U1 pad 12: /OUT_A_ROW_6 -> /EXT_ROW_6
- U1 pad 13: /OUT_A_ROW_5 -> /EXT_ROW_5
- U1 pad 14: /OUT_A_ROW_4 -> /EXT_ROW_4
- U1 pad 15: /OUT_A_ROW_3 -> /EXT_ROW_3
- U1 pad 16: /OUT_A_ROW_2 -> /EXT_ROW_2
- U1 pad 17: /OUT_A_ROW_1 -> /EXT_ROW_1
- U1 pad 18: /OUT_A_ROW_0 -> /EXT_ROW_0
- U1 pad 2: /EXT_ROW_0 -> /OUT_A_ROW_0
- U1 pad 3: /EXT_ROW_1 -> /OUT_A_ROW_1
- U1 pad 4: /EXT_ROW_2 -> /OUT_A_ROW_2
- U1 pad 5: /EXT_ROW_3 -> /OUT_A_ROW_3
- U1 pad 6: /EXT_ROW_4 -> /OUT_A_ROW_4
- U1 pad 7: /EXT_ROW_5 -> /OUT_A_ROW_5
- U1 pad 8: /EXT_ROW_6 -> /OUT_A_ROW_6
- U1 pad 9: /EXT_ROW_7 -> /OUT_A_ROW_7
- U3 pad 11: /OUT_A_COL_7 -> /EXT_COL_0
- U3 pad 12: /OUT_A_COL_6 -> /EXT_COL_1
- U3 pad 13: /OUT_A_COL_5 -> /EXT_COL_2
- U3 pad 14: /OUT_A_COL_4 -> /EXT_COL_3
- U3 pad 15: /OUT_A_COL_3 -> /EXT_COL_4
- U3 pad 16: /OUT_A_COL_2 -> /EXT_COL_5
- U3 pad 17: /OUT_A_COL_1 -> /EXT_COL_6
- U3 pad 18: /OUT_A_COL_0 -> /EXT_COL_7
- U3 pad 2: /EXT_COL_0 -> /OUT_A_COL_7
- U3 pad 3: /EXT_COL_1 -> /OUT_A_COL_6
- U3 pad 4: /EXT_COL_2 -> /OUT_A_COL_5
- U3 pad 5: /EXT_COL_3 -> /OUT_A_COL_4
- U3 pad 6: /EXT_COL_4 -> /OUT_A_COL_3
- U3 pad 7: /EXT_COL_5 -> /OUT_A_COL_2
- U3 pad 8: /EXT_COL_6 -> /OUT_A_COL_1
- U3 pad 9: /EXT_COL_7 -> /OUT_A_COL_0
- U5 pad 11: /OUT_B_ROW_7 -> /EXT_ROW_7
- U5 pad 12: /OUT_B_ROW_6 -> /EXT_ROW_6
- U5 pad 13: /OUT_B_ROW_5 -> /EXT_ROW_5
- U5 pad 14: /OUT_B_ROW_4 -> /EXT_ROW_4
- U5 pad 15: /OUT_B_ROW_3 -> /EXT_ROW_3
- U5 pad 16: /OUT_B_ROW_2 -> /EXT_ROW_2
- U5 pad 17: /OUT_B_ROW_1 -> /EXT_ROW_1
- U5 pad 18: /OUT_B_ROW_0 -> /EXT_ROW_0
- U5 pad 2: /EXT_ROW_0 -> /OUT_B_ROW_0
- U5 pad 3: /EXT_ROW_1 -> /OUT_B_ROW_1
- U5 pad 4: /EXT_ROW_2 -> /OUT_B_ROW_2
- U5 pad 5: /EXT_ROW_3 -> /OUT_B_ROW_3
- U5 pad 6: /EXT_ROW_4 -> /OUT_B_ROW_4
- U5 pad 7: /EXT_ROW_5 -> /OUT_B_ROW_5
- U5 pad 8: /EXT_ROW_6 -> /OUT_B_ROW_6
- U5 pad 9: /EXT_ROW_7 -> /OUT_B_ROW_7
- U7 pad 11: /OUT_B_COL_7 -> /EXT_COL_0
- U7 pad 12: /OUT_B_COL_6 -> /EXT_COL_1
- U7 pad 13: /OUT_B_COL_5 -> /EXT_COL_2
- U7 pad 14: /OUT_B_COL_4 -> /EXT_COL_3
- U7 pad 15: /OUT_B_COL_3 -> /EXT_COL_4
- U7 pad 16: /OUT_B_COL_2 -> /EXT_COL_5
- U7 pad 17: /OUT_B_COL_1 -> /EXT_COL_6
- U7 pad 18: /OUT_B_COL_0 -> /EXT_COL_7
- U7 pad 2: /EXT_COL_0 -> /OUT_B_COL_7
- U7 pad 3: /EXT_COL_1 -> /OUT_B_COL_6
- U7 pad 4: /EXT_COL_2 -> /OUT_B_COL_5
- U7 pad 5: /EXT_COL_3 -> /OUT_B_COL_4
- U7 pad 6: /EXT_COL_4 -> /OUT_B_COL_3
- U7 pad 7: /EXT_COL_5 -> /OUT_B_COL_2
- U7 pad 8: /EXT_COL_6 -> /OUT_B_COL_1
- U7 pad 9: /EXT_COL_7 -> /OUT_B_COL_0
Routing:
- net /BANK_SEL: track 39.4 -> 154.5 mm, vias 4 -> 6
- net /~{CURSOR_ROW_WTM}: track 0.00 -> 112.9 mm, vias 0 -> 4
- net /~{BANK_SEL}: track 48.1 -> 159.3 mm, vias 2 -> 4
- net /DATA_BUS_0: track 143.5 -> 235.3 mm, vias 0 -> 6
- net /DATA_BUS_1: track 126.1 -> 215.7 mm, vias 0 -> 7
- net /DATA_BUS_2: track 99.0 -> 185.1 mm, vias 0 -> 7
- net /DATA_CLK: track 0.00 -> 85.5 mm, vias 0 -> 2
- net /DATA_BUS_3: track 82.7 -> 165.9 mm, vias 0 -> 11
- net /DATA_BUS_4: track 77.9 -> 157.5 mm, vias 0 -> 7
- net /DATA_BUS_5: track 94.0 -> 166.3 mm, vias 0 -> 7
- net /DATA_BUS_6: track 121.3 -> 187.3 mm, vias 0 -> 7
- net /DATA_BUS_7: track 138.1 -> 198.1 mm, vias 0 -> 7
- net /~{CURSOR_ROW_RFM}: track 35.6 -> 90.6 mm
- net /~{CURSOR_COL_RFM}: track 12.0 -> 35.6 mm
- net /~{CURSOR_COL_WTM}: track 0.00 -> 18.2 mm
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
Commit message: First pass of video bank sel PCB complete.
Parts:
- removed C1: C, Capacitor_THT:C_Disc_D5.0mm_W2.5mm_P5.00mm
- removed R1: R_US, Resistor_THT:R_Axial_DIN0207_L6.3mm_D2.5mm_P10.16mm_Horizontal
- removed TP1: TestPoint, Connector_Pin:Pin_D1.0mm_L10.0mm
- moved C98 88.0 mm to (205.7, 91.4)
- moved C97 86.3 mm to (94.0, 94.0), turned to 180 degrees
- moved C99 46.8 mm to (63.5, 124.5), turned to 180 degrees
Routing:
- net VCC: track 180.0 -> 471.2 mm, vias 8 -> 9
- net /BANK_SEL: track 154.5 -> 324.5 mm, vias 6 -> 13
- net /~{BANK_SEL}: track 159.3 -> 325.6 mm, vias 4 -> 9
- net (no net): track 99.6 -> 0.00 mm
- net /~{CURSOR_COL_WTM}: track 18.2 -> 107.5 mm
- net /DATA_CLK: track 85.5 -> 159.6 mm, vias 2 -> 4
- net /EXT_ROW_0: track 12.4 -> 86.3 mm
- net /~{CURSOR_ROW_RFM}: track 90.6 -> 163.6 mm, vias 0 -> 4
- net /MEM_ACT: track 0.00 -> 71.9 mm, vias 0 -> 3
- net /~{RFM}/WTM: track 0.00 -> 67.5 mm, vias 0 -> 5
- net /EXT_ROW_1: track 12.4 -> 79.1 mm
- net /CURSOR_ROW_ADDRESSED: track 0.00 -> 61.4 mm, vias 0 -> 1
- net /CURSOR_COL_ADDRESSED: track 0.00 -> 61.4 mm, vias 0 -> 3
- net /EXT_ROW_2: track 12.4 -> 73.4 mm
- net /~{CURSOR_ROW_WTM}: track 112.9 -> 171.3 mm, vias 4 -> 6
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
